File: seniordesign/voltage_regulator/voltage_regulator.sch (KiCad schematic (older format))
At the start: 8 parts, among them J1 USB, U1 TPS62133

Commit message: voltage_regulator is fully footprinted!
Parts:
- R1: symbol R -> R-RESCUE-voltage_regulator
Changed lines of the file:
@@
 EESchema Schematic File Version 2
+LIBS:voltage_regulator-rescue
 LIBS:power
 LIBS:device
@@
 $EndDescr
 $Comp
-L TPS62133 U1
-U 1 1 55363C02
-P 2550 1850
-F 0 "U1" H 2550 1850 60  0000 C CNN
-F 1 "TPS62133" H 2550 2500 60  0000 C CNN
-F 2 "Housings_DFN_QFN:QFN-16-1EP_3x3mm_Pitch0.5mm" H 2550 1850 60  0001 C CNN
-F 3 "" H 2550 1850 60  0000 C CNN
-	1    2550 1850
-	1    0    0    -1
-$EndComp
-$Comp
 L C_Small C2
 U 1 1 553652BE
@@
 $EndComp
 $Comp
-L R R1
+L R-RESCUE-voltage_regulator R1
 U 1 1 553655ED
 P 4150 1450
@@
 $EndComp
 $Comp
-L GND #PWR02
+L GND-RESCUE-voltage_regulator #PWR02
 U 1 1 55378C9A
 P 1100 2100
@@
 $EndComp
 $Comp
-L GND #PWR03
+L GND-RESCUE-voltage_regulator #PWR03
 U 1 1 55378DC0
 P 2450 2900
@@
 $EndComp
 $Comp
-L GND #PWR04
+L GND-RESCUE-voltage_regulator #PWR04
 U 1 1 55378E2A
 P 1450 2450
@@
 $EndComp
 $Comp
-L GND #PWR05
+L GND-RESCUE-voltage_regulator #PWR05
 U 1 1 55378FAD
 P 4650 1650
@@
 $EndComp
 $Comp
-L GND #PWR06
+L GND-RESCUE-voltage_regulator #PWR06
 U 1 1 55378FD1
 P 5700 1500
@@
 	1    0    0    -1
 $EndComp
+$Comp
+L TPS62133 U1
+U 1 1 55DAB52A
+P 2550 1850
+F 0 "U1" H 2550 1850 60  0000 C CNN
+F 1 "TPS62133" H 2550 2500 60  0000 C CNN
+F 2 "Housings_DFN_QFN:QFN-16-1EP_3x3mm_Pitch0.5mm" H 2550 1850 60  0001 C CNN
+F 3 "" H 2550 1850 60  0000 C CNN
+	1    2550 1850
+	1    0    0    -1
+$EndComp

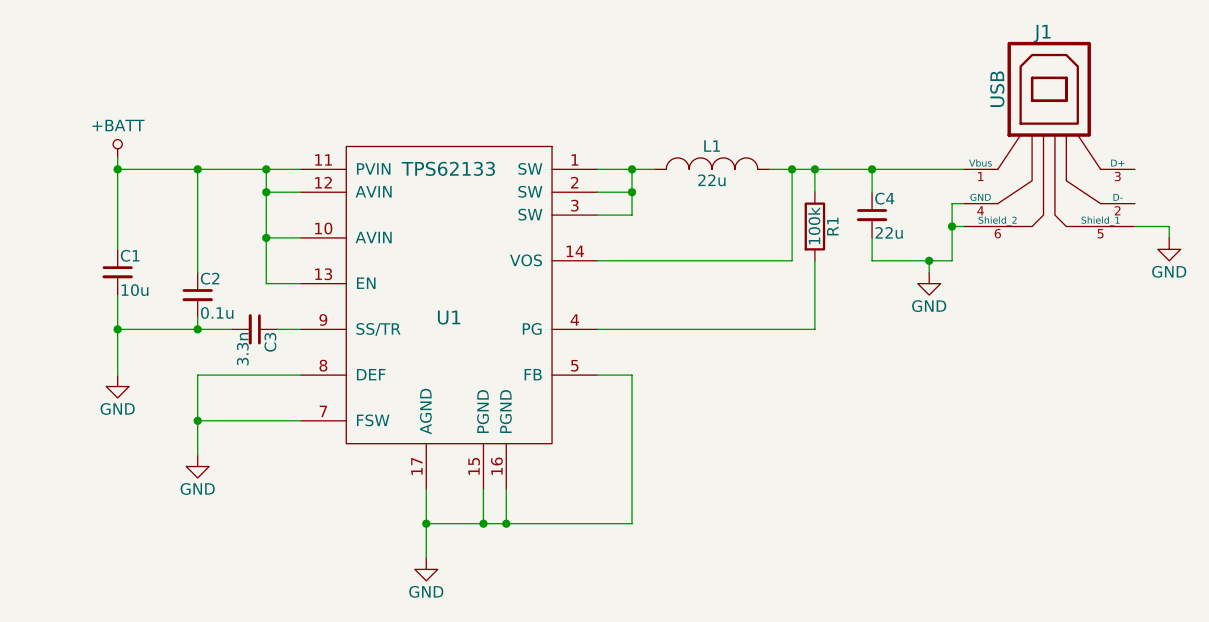
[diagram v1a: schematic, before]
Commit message: Generate PCB/Gerber files for voltage regulator circuit
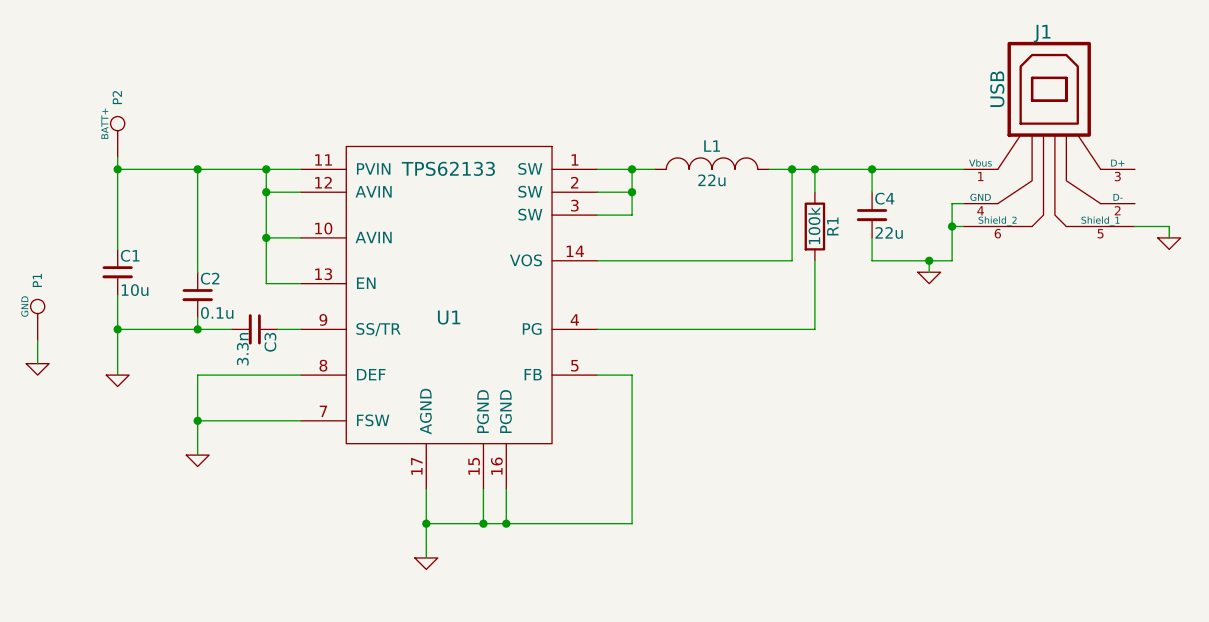
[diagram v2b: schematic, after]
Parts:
- added P1: GND, Connect:1pin, symbol CONN_1
- added P2: BATT+, Connect:1pin, symbol CONN_1
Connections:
- net GND: now also P1.1
- net +BATT: no longer names the net of C1.1, C2.1, U1.10 (AVIN), U1.11 (PVIN), U1.12 (AVIN), U1.13 (EN)
- net +BATT: now also P2.1
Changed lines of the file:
@@
 Connection ~ 1100 1900
-$Comp
-L +BATT #PWR01
-U 1 1 5537899D
-P 1100 1150
-F 0 "#PWR01" H 1100 1000 50  0001 C CNN
-F 1 "+BATT" H 1100 1290 50  0000 C CNN
-F 2 "Connect:1pin" H 1100 1150 60  0001 C CNN
-F 3 "" H 1100 1150 60  0000 C CNN
-	1    1100 1150
-	1    0    0    -1
-$EndComp
-$Comp
-L GND-RESCUE-voltage_regulator #PWR02
-U 1 1 55378C9A
-P 1100 2100
-F 0 "#PWR02" H 1100 1850 50  0001 C CNN
-F 1 "GND" H 1100 1950 50  0000 C CNN
-F 2 "Connect:1pin" H 1100 2100 60  0001 C CNN
-F 3 "" H 1100 2100 60  0000 C CNN
-	1    1100 2100
-	1    0    0    -1
-$EndComp
-$Comp
-L GND-RESCUE-voltage_regulator #PWR03
-U 1 1 55378DC0
-P 2450 2900
-F 0 "#PWR03" H 2450 2650 50  0001 C CNN
-F 1 "GND" H 2450 2750 50  0000 C CNN
-F 2 "" H 2450 2900 60  0000 C CNN
-F 3 "" H 2450 2900 60  0000 C CNN
-	1    2450 2900
-	1    0    0    -1
-$EndComp
-$Comp
-L GND-RESCUE-voltage_regulator #PWR04
-U 1 1 55378E2A
-P 1450 2450
-F 0 "#PWR04" H 1450 2200 50  0001 C CNN
-F 1 "GND" H 1450 2300 50  0000 C CNN
-F 2 "" H 1450 2450 60  0000 C CNN
-F 3 "" H 1450 2450 60  0000 C CNN
-	1    1450 2450
-	1    0    0    -1
-$EndComp
-$Comp
-L GND-RESCUE-voltage_regulator #PWR05
-U 1 1 55378FAD
-P 4650 1650
-F 0 "#PWR05" H 4650 1400 50  0001 C CNN
-F 1 "GND" H 4650 1500 50  0000 C CNN
-F 2 "" H 4650 1650 60  0000 C CNN
-F 3 "" H 4650 1650 60  0000 C CNN
-	1    4650 1650
-	1    0    0    -1
-$EndComp
-$Comp
-L GND-RESCUE-voltage_regulator #PWR06
-U 1 1 55378FD1
-P 5700 1500
-F 0 "#PWR06" H 5700 1250 50  0001 C CNN
-F 1 "GND" H 5700 1350 50  0000 C CNN
-F 2 "" H 5700 1500 60  0000 C CNN
-F 3 "" H 5700 1500 60  0000 C CNN
-	1    5700 1500
-	1    0    0    -1
-$EndComp
 $Comp
 L TPS62133 U1
@@
 	1    0    0    -1
 $EndComp
+$Comp
+L GND #PWR2
+U 1 1 55DC6EC3
+P 1100 2100
+F 0 "#PWR2" H 1100 2100 30  0001 C CNN
+F 1 "GND" H 1100 2030 30  0001 C CNN
+F 2 "Connect:1pin" H 1100 2100 60  0001 C CNN
+F 3 "" H 1100 2100 60  0000 C CNN
+	1    1100 2100
+	1    0    0    -1
+$EndComp
+$Comp
+L GND #PWR3
+U 1 1 55DC6EFE
+P 1450 2450
+F 0 "#PWR3" H 1450 2450 30  0001 C CNN
+F 1 "GND" H 1450 2380 30  0001 C CNN
+F 2 "" H 1450 2450 60  0000 C CNN
+F 3 "" H 1450 2450 60  0000 C CNN
+	1    1450 2450
+	1    0    0    -1
+$EndComp
+$Comp
+L GND #PWR4
+U 1 1 55DC6F62
+P 2450 2900
+F 0 "#PWR4" H 2450 2900 30  0001 C CNN
+F 1 "GND" H 2450 2830 30  0001 C CNN
+F 2 "" H 2450 2900 60  0000 C CNN
+F 3 "" H 2450 2900 60  0000 C CNN
+	1    2450 2900
+	1    0    0    -1
+$EndComp
+$Comp
+L GND #PWR5
+U 1 1 55DC6FA7
+P 4650 1650
+F 0 "#PWR5" H 4650 1650 30  0001 C CNN
+F 1 "GND" H 4650 1580 30  0001 C CNN
+F 2 "" H 4650 1650 60  0000 C CNN
+F 3 "" H 4650 1650 60  0000 C CNN
+	1    4650 1650
+	1    0    0    -1
+$EndComp
+$Comp
+L GND #PWR6
+U 1 1 55DC6FCA
+P 5700 1500
+F 0 "#PWR6" H 5700 1500 30  0001 C CNN
+F 1 "GND" H 5700 1430 30  0001 C CNN
+F 2 "" H 5700 1500 60  0000 C CNN
+F 3 "" H 5700 1500 60  0000 C CNN
+	1    5700 1500
+	1    0    0    -1
+$EndComp
+$Comp
+L CONN_1 P2
+U 1 1 55DC745F
+P 1100 1000
+F 0 "P2" H 1180 1000 40  0000 L CNN
+F 1 "BATT+" H 1100 1055 30  0000 C CNN
+F 2 "Connect:1pin" H 1100 1000 60  0001 C CNN
+F 3 "" H 1100 1000 60  0000 C CNN
+	1    1100 1000
+	0    -1   -1   0
+$EndComp
+$Comp
+L CONN_1 P1
+U 1 1 55DC75EC
+P 750 1800
+F 0 "P1" H 830 1800 40  0000 L CNN
+F 1 "GND" H 750 1855 30  0000 C CNN
+F 2 "Connect:1pin" H 750 1800 60  0001 C CNN
+F 3 "" H 750 1800 60  0000 C CNN
+	1    750  1800
+	0    -1   -1   0
+$EndComp
+$Comp
+L GND #PWR1
+U 1 1 55DC76D5
+P 750 2050
+F 0 "#PWR1" H 750 2050 30  0001 C CNN
+F 1 "GND" H 750 1980 30  0001 C CNN
+F 2 "Connect:1pin" H 750 2050 60  0001 C CNN
+F 3 "" H 750 2050 60  0000 C CNN
+	1    750  2050
+	1    0    0    -1
+$EndComp
+Wire Wire Line
+	750  1950 750  2050
 $EndSCHEMATC
